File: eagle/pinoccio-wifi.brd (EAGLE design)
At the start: 25.4 x 55.5 mm, 13 parts, among them U1 V_REG_LDOSMD

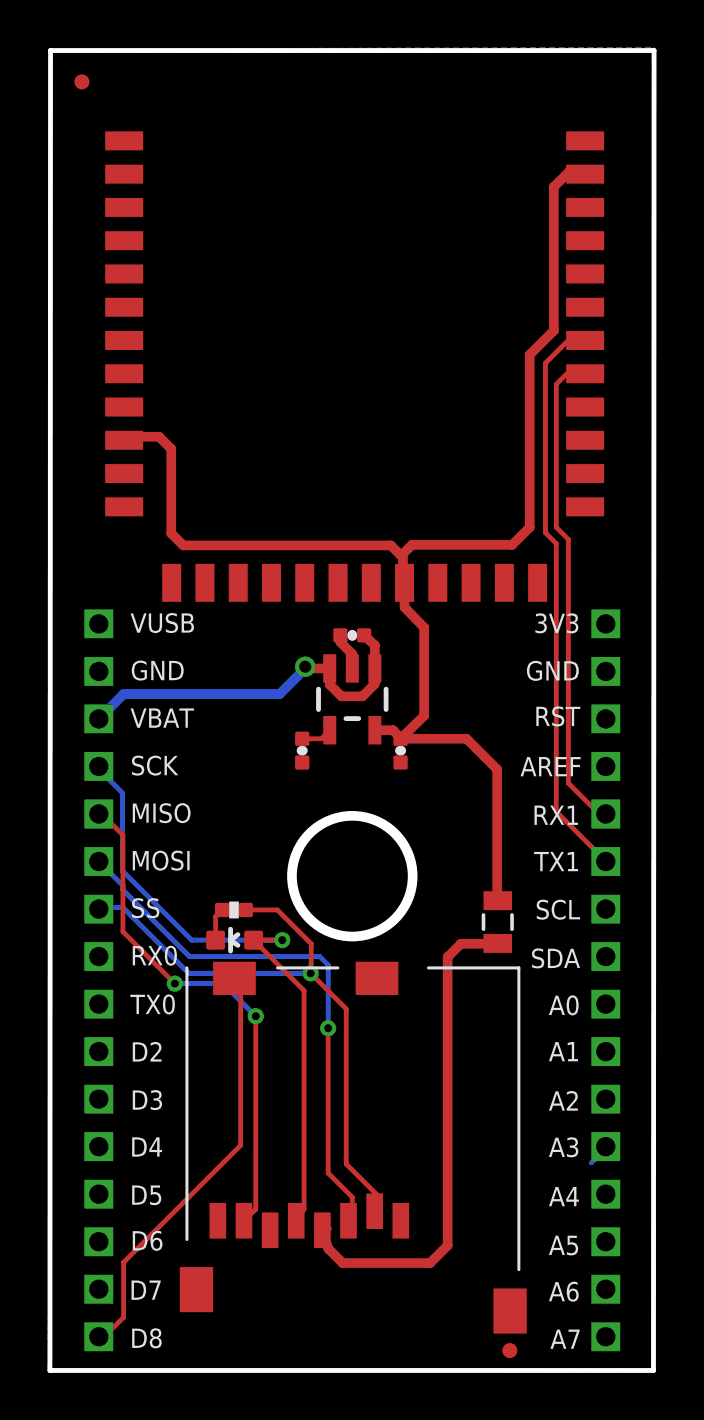
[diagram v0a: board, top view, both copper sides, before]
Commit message: More fixups to capacitor design error and lack of enable
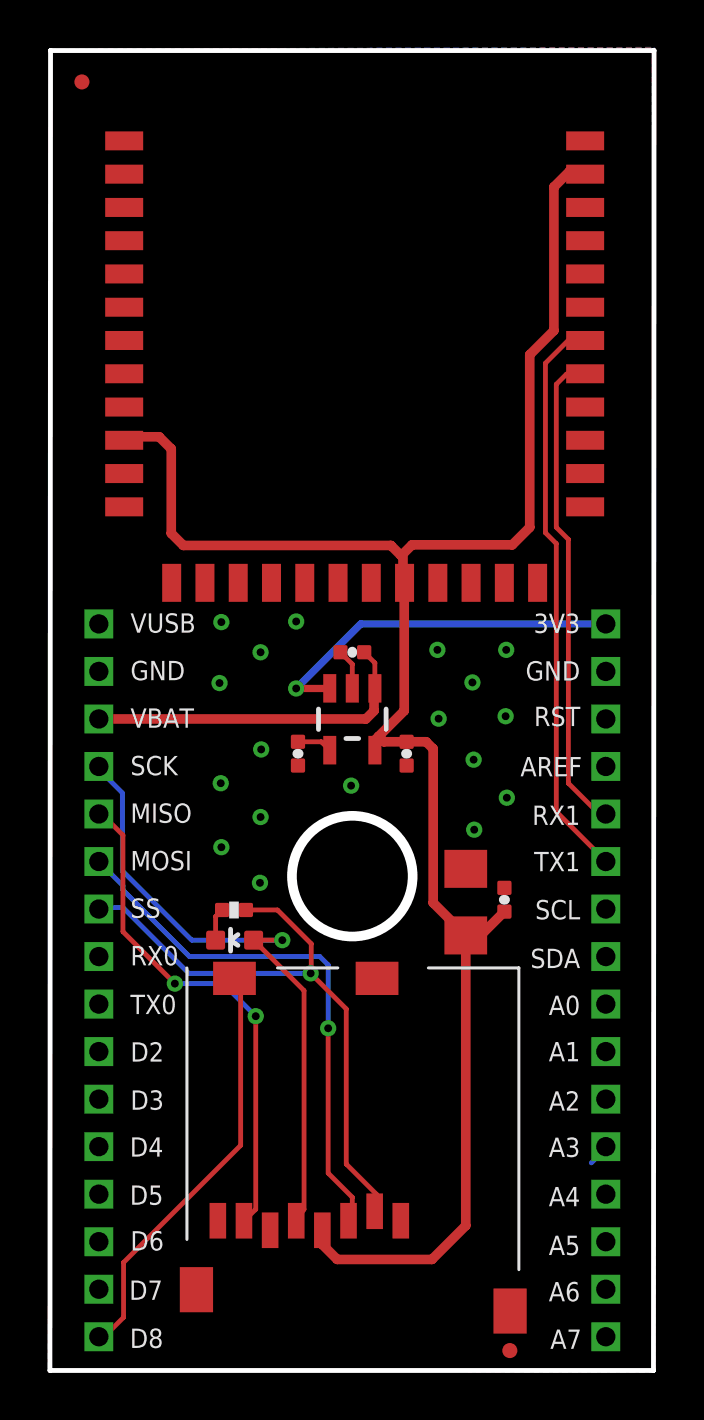
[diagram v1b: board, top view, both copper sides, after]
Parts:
- added C4: 0.1uf, Pinoccio:0402-CAP
- C5: value 22uf -> 10uf; device Pinoccio:0805 -> Pinoccio:1206
- moved C5 1.59 mm to (17.5, 27.7)
- moved U1 0.84 mm to (12.7, 35.4)
- moved C1 0.71 mm to (12.7, 38.2)
- moved C2 0.28 mm to (15.0, 33.9)
- moved C3 0.22 mm to (10.4, 33.9)
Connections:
- removed net VDD: C5.1, U$1.4
- net GND: now also C4.2, C5.2
- net VBAT-AF: no longer U1.3
- net VCC: now also C4.1, C5.1, U$1.4; no longer C5.2
- net VCC-AE: now also U1.3
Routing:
- net VDD: track 21.6 -> 0.00 mm
- net VCC: track 58.4 -> 80.0 mm
- net VCC-AE: track 0.00 -> 15.6 mm, vias 0 -> 1
- net VBAT-AF: track 16.0 -> 14.4 mm, vias 1 -> 0
- net GND: track 1.60 -> 1.73 mm, vias 0 -> 18

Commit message: Revision v0.9
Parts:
- removed LED3: Red, Pinoccio:LED-0603
- removed R3: 1k, Pinoccio:0402-RES
- added C6: 2.2uf, Pinoccio:0402-CAP
- added D1, D2: (no value), Pinoccio:0603-DIODE
- added U$2: M25PX16, Pinoccio:SO8N
- added U2: LDO-TPS73533, Pinoccio:SON-6-DRV
- C2: value 4.7uf -> 2.2uf
- C3: value 0.01uf -> 1.0uf
- U1: value V_REG_LDOSMD -> LDO-TPS78233; device Pinoccio:SOT23-5 -> Pinoccio:SON-6-DRV
- moved C3 7.55 mm to (17.9, 33.4), turned to 180 degrees
- moved U1 4.69 mm to (16.5, 32.6), turned to 270 degrees
- moved C1 3.67 mm to (16.3, 37.4)
- moved C2 1.67 mm to (14.0, 35.3)
- moved C4 1.16 mm to (20.1, 28.4), turned to 0 degrees
- moved C5 0.14 mm to (17.5, 27.8), turned to 270 degrees
- moved U$1 0.13 mm to (5.74, 25.0)
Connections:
- removed net D7: JP-L.P$15
- removed net D8: JP-L.P$16, U$1.CD1
- removed net N$3: LED3.C, R3.1
- removed net VBAT-AF: C1.1, JP-L.P$3, U1.1
- removed net VCC: C2.1, C4.1, C5.1, GS1011MIPS.P$10, GS1011MIPS.P$20, GS1011MIPS.P$35, U$1.4, U1.5
- new net D0: JP-L.P$10
- new net D1: JP-L.P$11
- new net MEM-VCC: C4.1, C5.1, C6.1, U$1.4, U$2.8, U1.P$1
- new net VBAT-AE: C1.1, C3.1, JP-R.P$3, U1.P$6, U2.P$6
- new net WIFI-EN: GS1011MIPS.P$12, U2.P$4
- new net WIFI-VCC: C2.1, D1.A, GS1011MIPS.P$20, U2.P$1
- net AREF: now also JP-R.P$8; no longer JP-R.P$4
- net D2: now also JP-L.P$12; no longer JP-L.P$10
- net D3: now also JP-L.P$13; no longer JP-L.P$11
- net D4: now also JP-L.P$14, U$1.CD1; no longer JP-L.P$12
- net D5: now also JP-L.P$15, U$1.2; no longer JP-L.P$13
- net D6: now also GS1011MIPS.P$9, JP-L.P$16; no longer JP-L.P$14
- net GND: now also C6.2, U$2.4, U1.P$3, U1.P$5, U1.P$7, U2.P$3, U2.P$7; no longer U1.2
- net MISO: now also U$2.2
- net MOSI: now also U$2.5
- net N$2: now also D1.C, D2.C, GS1011MIPS.P$10, GS1011MIPS.P$35; no longer C3.1, U1.4
- net RESET: now also JP-L.P$3; no longer JP-R.P$3
- net RX1: now also JP-R.P$4; no longer JP-R.P$5
- net SCK: now also U$2.6; no longer LED3.A
- net SCL: now also JP-R.P$6; no longer JP-R.P$7
- net SDA: now also JP-R.P$7; no longer JP-R.P$8
- net SSN: now also U$2.1; no longer R3.2, U$1.2
- net TX1: now also JP-R.P$5; no longer JP-R.P$6
- net VCC-AE: now also D2.A, U1.P$4; no longer U1.3
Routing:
- net VCC: track 80.0 -> 0.00 mm
- net MEM-VCC: track 0.00 -> 44.7 mm, vias 0 -> 2
- net N$2: track 1.48 -> 44.0 mm, vias 0 -> 2
- net D6: track 0.00 -> 40.9 mm
- net WIFI-EN: track 0.00 -> 19.6 mm, vias 0 -> 2
- net D8: track 18.2 -> 0.00 mm
- net MOSI: track 22.8 -> 40.8 mm, vias 1 -> 3
- net SSN: track 25.9 -> 7.88 mm, vias 1 -> 0
- net D5: track 0.00 -> 17.0 mm, vias 0 -> 2
- net D4: track 0.00 -> 15.4 mm, vias 0 -> 1
- net VBAT-AF: track 14.4 -> 0.00 mm
- net VBAT-AE: track 0.00 -> 11.6 mm
- net SCK: track 26.7 -> 37.5 mm, vias 1 -> 3
- net WIFI-VCC: track 0.00 -> 7.39 mm
- net MISO: track 21.3 -> 27.1 mm, vias 2 -> 1
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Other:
- board text added: "D0"
- board text added: "D1"
- board text removed: "D7"
- board text removed: "D8"

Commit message: Moar fixups
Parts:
- added U$3: PAD, Pinoccio:0.1-PAD
- U1: device Pinoccio:SON-6-DRV -> Pinoccio:SOT23-5
- moved C3 3.65 mm to (20.1, 30.4), turned to 0 degrees
- moved C1 1.58 mm to (17.9, 37.4), turned to 0 degrees
- moved C6 0.92 mm to (14.5, 32.9)
- moved U1 0.83 mm to (17.1, 32.1), turned to 90 degrees
- moved C5 0.10 mm to (17.4, 27.8)
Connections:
- new net PGM_MODE: GS1011MIPS.P$26, U$3.P$1
- net GND: now also U1.2, U1.4; no longer U1.P$3, U1.P$5, U1.P$7
- net MEM-VCC: now also U1.5; no longer U1.P$1
- net VBAT-AE: now also U1.1; no longer U1.P$6
- net VCC-AE: now also U1.3; no longer U1.P$4
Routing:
- net PGM_MODE: track 0.00 -> 16.8 mm
- net VBAT-AE: track 11.6 -> 16.5 mm
- net GND: track 6.22 -> 2.09 mm, vias 30 -> 33
- net MEM-VCC: track 44.7 -> 42.2 mm
- net SCK: track 37.5 -> 35.5 mm
- net D5: track 17.0 -> 15.2 mm, vias 2 -> 1
- net VCC-AE: track 15.5 -> 13.9 mm
- net MOSI: track 40.8 -> 40.1 mm
- net D4: track 15.4 -> 14.6 mm, vias 1 -> 0

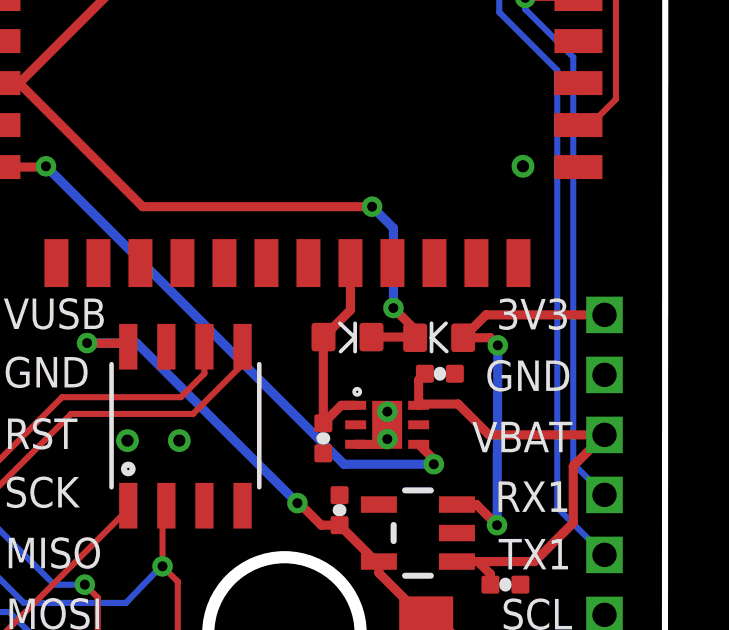
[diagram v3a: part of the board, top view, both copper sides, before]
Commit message: Update datasheet and dioide layout to 0603
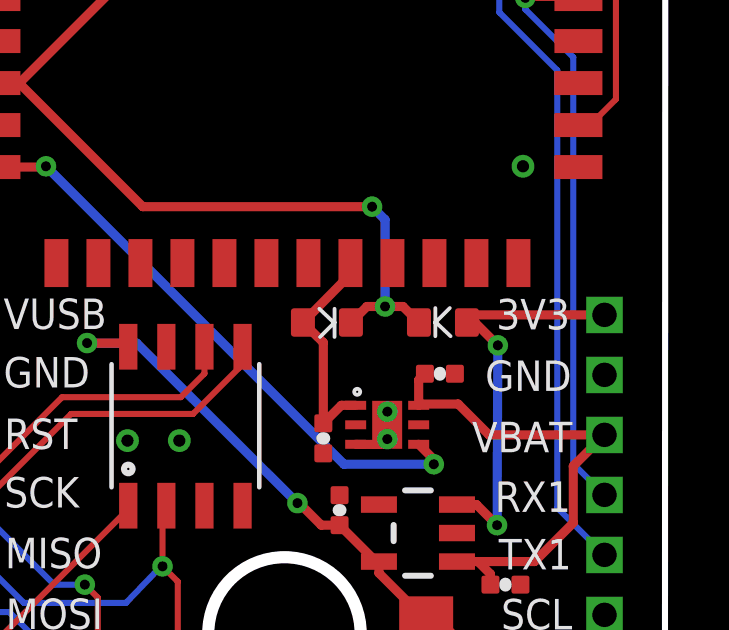
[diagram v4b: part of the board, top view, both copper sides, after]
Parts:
- D1, D2: value (none) -> DIODE-SCHOTTKY
- moved D1 0.84 mm to (14.1, 39.1)
- moved D2 0.52 mm to (18.0, 39.1)
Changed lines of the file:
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@@
 <attribute name="VALUE" x="18.9865" y="27.2542" size="0.4064" layer="27"/>
 </element>
-<element name="D1" library="Pinoccio" package="0603-DIODE" value="" x="14.8012" y="38.6304" smashed="yes">
-<attribute name="VALUE" x="13.7852" y="37.4874" size="0.4064" layer="27" font="vector"/>
-</element>
-<element name="D2" library="Pinoccio" package="0603-DIODE" value="" x="17.8562" y="38.608" smashed="yes" rot="R180">
-<attribute name="VALUE" x="18.8722" y="39.751" size="0.4064" layer="27" font="vector" rot="R180"/>
+<element name="D1" library="Pinoccio" package="0603-DIODE" value="DIODE-SCHOTTKY" x="14.1154" y="39.116" smashed="yes">
+<attribute name="VALUE" x="13.0994" y="37.973" size="0.4064" layer="27" font="vector"/>
+</element>
+<element name="D2" library="Pinoccio" package="0603-DIODE" value="DIODE-SCHOTTKY" x="17.9832" y="39.116" smashed="yes" rot="R180">
+<attribute name="VALUE" x="18.9992" y="40.259" size="0.4064" layer="27" font="vector" rot="R180"/>
 </element>
 <element name="C3" library="Pinoccio" package="0402-CAP" value="1.0uf" x="20.066" y="30.3784" smashed="yes">
@@
 <wire x1="15.0742" y1="36.3558" x2="14.596" y2="36.3558" width="0.3048" layer="1"/>
 <wire x1="14.596" y1="36.3558" x2="13.9954" y2="35.7552" width="0.3048" layer="1"/>
-<wire x1="14.0012" y1="38.6304" x2="14.8988" y2="39.528" width="0.3048" layer="1"/>
-<wire x1="14.8988" y1="39.528" x2="14.8988" y2="41.0972" width="0.3048" layer="1"/>
-<wire x1="14.0012" y1="38.6304" x2="13.9954" y2="38.8024" width="0.3048" layer="1"/>
-<wire x1="13.9954" y1="38.8024" x2="13.9954" y2="35.7552" width="0.3048" layer="1"/>
+<wire x1="13.3154" y1="39.116" x2="13.9954" y2="38.4468" width="0.3048" layer="1"/>
+<wire x1="13.9954" y1="38.4468" x2="13.9954" y2="35.7552" width="0.3048" layer="1"/>
+<wire x1="13.3154" y1="39.116" x2="14.8988" y2="40.7218" width="0.3048" layer="1"/>
+<wire x1="14.8988" y1="40.7218" x2="14.8988" y2="41.0972" width="0.3048" layer="1"/>
 </signal>
 <signal name="MOSI">
@@
 <contactref element="U1" pad="1"/>
 <contactref element="U2" pad="P$6"/>
-<wire x1="23.368" y1="35.37" x2="19.5194" y2="35.37" width="0.3048" layer="1"/>
 <wire x1="19.5194" y1="35.37" x2="18.4912" y2="36.3982" width="0.3048" layer="1"/>
 <wire x1="18.4912" y1="36.3982" x2="17.2166" y2="36.3982" width="0.3048" layer="1"/>
@@
 <wire x1="17.3816" y1="37.4076" x2="17.1742" y2="37.2002" width="0.3048" layer="1"/>
 <wire x1="17.1742" y1="37.2002" x2="17.1742" y2="36.3558" width="0.3048" layer="1"/>
+<wire x1="23.368" y1="35.37" x2="19.5194" y2="35.37" width="0.3048" layer="1"/>
 </signal>
 <signal name="SSN">
@@
 <contactref element="U1" pad="3"/>
 <via x="19.7866" y="32.3596" extent="1-16" drill="0.3302"/>
-<wire x1="18.6562" y1="38.608" x2="19.4182" y2="39.37" width="0.3048" layer="1"/>
-<wire x1="19.4182" y1="39.37" x2="23.368" y2="39.37" width="0.3048" layer="1"/>
+<wire x1="18.7832" y1="39.116" x2="19.0372" y2="39.37" width="0.3048" layer="1"/>
+<wire x1="19.0372" y1="39.37" x2="23.368" y2="39.37" width="0.3048" layer="1"/>
 <wire x1="19.7866" y1="32.3596" x2="19.812" y2="38.354" width="0.3048" layer="16"/>
 <via x="19.812" y="38.354" extent="1-16" drill="0.3302"/>
-<wire x1="19.812" y1="38.354" x2="19.558" y2="38.608" width="0.3048" layer="1"/>
-<wire x1="19.558" y1="38.608" x2="18.6562" y2="38.608" width="0.3048" layer="1"/>
+<wire x1="19.812" y1="38.354" x2="19.0754" y2="39.0906" width="0.3048" layer="1"/>
+<wire x1="19.0754" y1="39.0906" x2="18.7832" y2="39.116" width="0.3048" layer="1"/>
 <wire x1="19.0988" y1="33.0474" x2="19.7866" y2="32.3596" width="0.3048" layer="1"/>
 <wire x1="19.0988" y1="33.0474" x2="18.4499" y2="33.0474" width="0.3048" layer="1"/>
@@
 <wire x1="4.7498" y1="44.323" x2="4.724" y2="44.2972" width="0.3048" layer="1"/>
 <wire x1="4.724" y1="44.2972" x2="3.0988" y2="44.2972" width="0.3048" layer="1"/>
+<wire x1="14.6812" y1="34.3916" x2="17.6784" y2="34.3916" width="0.3048" layer="16"/>
 <wire x1="4.7498" y1="44.323" x2="14.6812" y2="34.3916" width="0.3048" layer="16"/>
-<wire x1="14.6812" y1="34.3916" x2="17.6784" y2="34.3916" width="0.3048" layer="16"/>
 </signal>
 <signal name="N$2">
@@
 <contactref element="D2" pad="C"/>
 <contactref element="D1" pad="C"/>
-<wire x1="17.0562" y1="38.608" x2="16.9262" y2="38.6304" width="0.3048" layer="1"/>
-<wire x1="16.9262" y1="38.6304" x2="15.6012" y2="38.6304" width="0.3048" layer="1"/>
 <wire x1="3.0988" y1="47.0972" x2="3.1044" y2="47.0916" width="0.3048" layer="1"/>
 <wire x1="3.1044" y1="47.0916" x2="3.8608" y2="47.0916" width="0.3048" layer="1"/>
@@
 <wire x1="7.9756" y1="42.9768" x2="15.621" y2="42.9768" width="0.3048" layer="1"/>
 <via x="15.621" y="42.9768" extent="1-16" drill="0.3302"/>
-<wire x1="15.621" y1="42.9768" x2="16.3322" y2="42.2656" width="0.3048" layer="16"/>
-<wire x1="16.3322" y1="42.2656" x2="16.3322" y2="39.5986" width="0.3048" layer="16"/>
-<via x="16.3322" y="39.5986" extent="1-16" drill="0.3302"/>
-<wire x1="16.3322" y1="39.5986" x2="17.107" y2="38.8238" width="0.3048" layer="1"/>
-<wire x1="17.107" y1="38.8238" x2="17.0562" y2="38.608" width="0.3048" layer="1"/>
+<wire x1="15.621" y1="42.9768" x2="16.0528" y2="42.545" width="0.3048" layer="16"/>
+<wire x1="16.0528" y1="42.545" x2="16.0528" y2="39.6494" width="0.3048" layer="16"/>
+<via x="16.0528" y="39.6494" extent="1-16" drill="0.3302"/>
+<wire x1="14.9154" y1="39.116" x2="15.4488" y2="39.6494" width="0.3048" layer="1"/>
+<wire x1="15.4488" y1="39.6494" x2="16.0528" y2="39.6494" width="0.3048" layer="1"/>
+<wire x1="17.1832" y1="39.116" x2="16.6498" y2="39.6494" width="0.3048" layer="1"/>
+<wire x1="16.6498" y1="39.6494" x2="16.0528" y2="39.6494" width="0.3048" layer="1"/>
 </signal>
 <signal name="MEM-VCC">

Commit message: v0.11 changes
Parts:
- removed D1, D2: DIODE-SCHOTTKY, Pinoccio:0603-DIODE
- removed U1: LDO-TPS78233, Pinoccio:SOT23-5
- added C7: 0.1uf, Pinoccio:0402-CAP
- added J1: AVR_SPI_PRG_6, Pinoccio:2X3-PAD
- added R2: 10k, Pinoccio:0402-RES
- added U$4: M25PX16SO8N, Pinoccio:SO8N
- C3: value 1.0uf -> 0.1uf
- C5: value 10uf -> 22uf; device Pinoccio:1206 -> Pinoccio:0603-CAP
- C6: value 2.2uf -> 0.1uf
- U$2: value M25PX16 -> M25PX16SO8N
- U$3: value PAD -> ATTINY13QFN10; device Pinoccio:0.1-PAD -> Pinoccio:QFN-10
- moved U$3 34.1 mm to (17.7, 28.1), turned to 90 degrees
- moved C1 13.6 mm to (9.29, 26.8), turned to 270 degrees
- moved C3 11.4 mm to (12.7, 39.1), turned to 270 degrees
- moved C6 10.5 mm to (5.59, 38.4), turned to 180 degrees
- moved C5 10.4 mm to (7.16, 26.1), turned to 180 degrees
- moved U2 8.81 mm to (9.15, 30.2), turned to 180 degrees
- moved U$2 6.26 mm to (15.6, 35.3)
- moved C2 6.13 mm to (9.42, 31.2), turned to 0 degrees
- moved C4 5.17 mm to (15.5, 25.9)
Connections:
- net USB_VIN renamed VBUS
- removed net D0: JP-L.P$10
- removed net D1: JP-L.P$11
- removed net MEM-VCC: C4.1, C5.1, C6.1, U$1.4, U$2.8, U1.5
- removed net PGM_MODE: GS1011MIPS.P$26, U$3.P$1
- removed net VBAT-AE: C1.1, C3.1, JP-R.P$3, U1.1, U2.P$6
- removed net WIFI-EN: GS1011MIPS.P$12, U2.P$4
- new net BKPK-BUS: J1.4, JP-L.P$2, U$3.6
- new net D7: GS1011MIPS.P$6, JP-L.P$15
- new net D8: JP-L.P$16, U$1.2
- new net MSPI-CS: GS1011MIPS.P$14, R2.2, U$4.1
- new net MSPI-MISO: GS1011MIPS.P$17, U$4.2
- new net MSPI-MOSI: GS1011MIPS.P$18, U$4.5
- new net MSPI-SCK: GS1011MIPS.P$15, U$4.6
- new net N$3: J1.3, U$3.9
- new net N$4: J1.5, U$3.1
- new net VBAT: C1.1, JP-R.P$3, U2.6
- net D2: now also JP-L.P$10; no longer JP-L.P$12
- net D3: now also JP-L.P$11; no longer JP-L.P$13
- net D4: now also JP-L.P$12; no longer JP-L.P$14, U$1.CD1
- net D5: now also JP-L.P$13; no longer JP-L.P$15, U$1.2
- net D6: now also GS1011MIPS.P$26, JP-L.P$14; no longer GS1011MIPS.P$9, JP-L.P$16
- net GND: now also C7.2, J1.6, U$3.5, U$3.EP, U$4.4, U2.3, U2.PAD; no longer JP-L.P$2, U1.2, U1.4, U2.P$3, U2.P$7
- net MISO: now also GS1011MIPS.P$8
- net MOSI: now also GS1011MIPS.P$5
- net N$2: now also J1.1, U$3.7; no longer D1.C, D2.C, GS1011MIPS.P$10, GS1011MIPS.P$35
- net SCK: now also GS1011MIPS.P$7
- net VCC-AE: now also C3.1, C4.1, C5.1, C7.1, GS1011MIPS.P$10, GS1011MIPS.P$35, J1.2, U$1.4, U$2.8, U$3.10, U2.4; no longer D2.A, U1.3
- net WIFI-VCC: now also C6.1, R2.1, U$4.8, U2.1; no longer D1.A, U2.P$1
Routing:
- net VCC-AE: track 13.6 -> 105.1 mm, vias 2 -> 5
- net MISO: track 27.1 -> 74.1 mm, vias 1 -> 5
- net D7: track 0.00 -> 43.6 mm, vias 0 -> 1
- net MEM-VCC: track 42.2 -> 0.00 mm, vias 2 -> 0
- net SCK: track 35.5 -> 74.0 mm, vias 3 -> 5
- net MOSI: track 40.1 -> 74.8 mm, vias 3 -> 4
- net VBAT: track 0.00 -> 28.4 mm, vias 0 -> 2
- net N$2: track 43.7 -> 18.1 mm, vias 2 -> 1
- net BKPK-BUS: track 0.00 -> 25.6 mm, vias 0 -> 1
- net N$4: track 0.00 -> 20.1 mm, vias 0 -> 1
- net WIFI-EN: track 19.6 -> 0.00 mm, vias 2 -> 0
- net WIFI-VCC: track 7.60 -> 26.6 mm, vias 0 -> 2
- net GND: track 2.09 -> 20.1 mm, vias 33 -> 15
- net PGM_MODE: track 16.8 -> 0.00 mm
- net VBAT-AE: track 16.5 -> 0.00 mm
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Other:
- board text added: "BAT"
- board text added: "BKPK"
- board text added: "D7"
- board text added: "D8"
- board text added: "Pinoccio(tm) WiFi Backpack v0.11"
- board text added: "RX"
- board text added: "TX"
- board text added: "USB"
- board text added: "wifi backpack v0.11"
- board text removed: "D0"
- board text removed: "D1"
- board text removed: "Pinoccio(tm) Wifi v0.9"
- board text removed: "RX0"
- board text removed: "TX0"
- board text removed: "VBAT"
- board text removed: "VUSB"
- board text removed: "pinoccio wi-fi v0.9"

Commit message: Updated board to v0.13
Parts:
- removed JP3, JP5: FIDUCIALUFIDUCIAL, Pinoccio:MICRO-FIDUCIAL
- moved U$2 1.09 mm to (15.6, 36.4)
- moved U$4 1.09 mm to (9.70, 36.4)
- moved C2 0.87 mm to (8.71, 31.7), turned to 90 degrees
- moved R2 0.58 mm to (6.55, 33.6)
- moved C7 0.53 mm to (16.8, 31.1)
- moved JP-R 0.38 mm to (23.7, 39.4)
- moved JP-L 0.38 mm to (1.65, 39.4)
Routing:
- net SSN: track 15.0 -> 17.1 mm
- net SCK: track 74.0 -> 75.3 mm
- net MISO: track 74.1 -> 75.2 mm
- net MSPI-MISO: track 9.33 -> 8.23 mm
- net MOSI: track 74.8 -> 75.6 mm
- net D6: track 48.2 -> 49.0 mm
- net MSPI-MOSI: track 3.40 -> 2.84 mm
- net VCC-AE: track 105.1 -> 105.7 mm
- net GND: track 20.1 -> 19.6 mm
- net MSPI-SCK: track 4.24 -> 3.72 mm
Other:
- board size 25.4 x 55.5 mm -> 25.4 x 55.4 mm
- board text added: "Pinoccio(tm) Wi-Fi Backpack v0.13"
- board text added: "tiny13A"
- board text added: "wi-fi backpack v0.13"
- board text removed: "Pinoccio(tm) WiFi Backpack v0.11"
- board text removed: "wifi backpack v0.11"
